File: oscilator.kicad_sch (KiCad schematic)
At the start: 5 parts, among them Y1 8Mhz

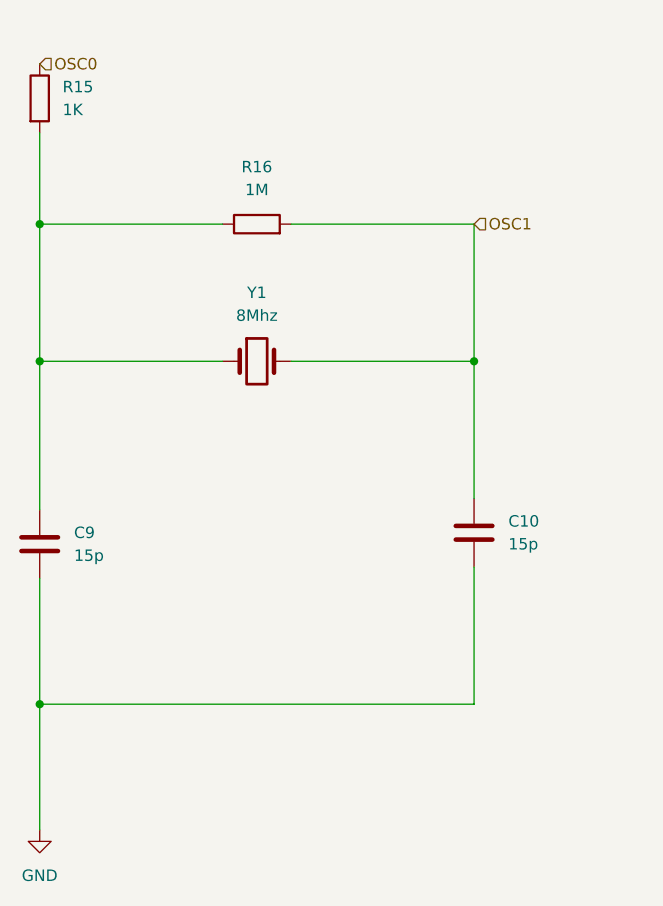
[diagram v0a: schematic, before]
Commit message: feat: PCB layout updates, schematic changes, fp-lib-table config
- cnc_pic32.kicad_pcb: component repositioning, board outline, text formatting
- cnc_pic32.kicad_prl/pro: project settings updates
- fp-lib-table: add Library path to Library.pretty
- mcu.kicad_sch: PIC32 pin configuration updates
- zigbee.kicad_sch: MRF24J40 module updates
- oscilator.kicad_sch: crystal configuration
- power.kicad_sch/power_ft232.kicad_sch: power supply updates
- oled.kicad_sch: OLED display connections
- idc.kicad_sch: IDC connector updates
- osc_ft232.kicad_sch: FT232 crystal
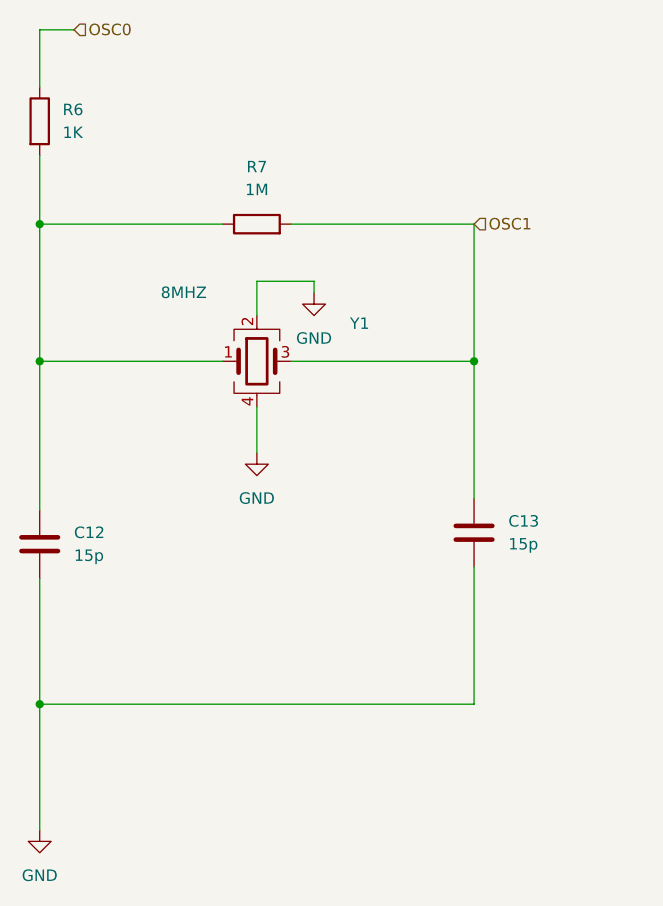
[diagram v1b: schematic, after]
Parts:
- removed Y1: 8Mhz, symbol Device:Crystal
- added Y1: 8MHZ, Crystal:Crystal_SMD_0603-4Pin_6.0x3.5mm, symbol Device:Crystal_GND24
- renumbered C9 to C12, C10 to C13, R15 to R6, R16 to R7
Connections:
- net GND: now also Y1.2, Y1.4
- net OSC1: now also Y1.3
- net at C12.1, R6.2, R7.1: now also Y1.1
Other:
- moved on the sheet: R6

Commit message: feat: integrate zigbee sheet + R 0603→0805 footprint update
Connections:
- net OSC0 renamed OSC2
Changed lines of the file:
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@@
 	(paper "A4")
 	(junction
+		(at 127 125.73)
+		(diameter 0)
+		(color 0 0 0 0)
+	)
+	(junction
+		(at 127 72.39)
+		(diameter 0)
+		(color 0 0 0 0)
+	)
+	(junction
 		(at 175.26 87.63)
 		(diameter 0)
@@
 	)
 	(junction
-		(at 127 125.73)
-		(diameter 0)
-		(color 0 0 0 0)
-	)
-	(junction
-		(at 127 72.39)
+		(at 175.26 72.39)
 		(diameter 0)
 		(color 0 0 0 0)
@@
 	(wire
 		(pts
+			(xy 175.26 62.23) (xy 175.26 72.39)
+		)
+		(stroke
+			(width 0)
+			(type default)
+		)
+	)
+	(wire
+		(pts
 			(xy 127 125.73) (xy 175.26 125.73)
 		)
@@
 		(pts
 			(xy 130.81 50.8) (xy 127 50.8)
+		)
+		(stroke
+			(width 0)
+			(type default)
+		)
+	)
+	(wire
+		(pts
+			(xy 175.26 62.23) (xy 186.69 62.23)
 		)
 		(stroke
@@
 	(hierarchical_label "OSC1"
 		(shape input)
-		(at 175.26 72.39 0)
+		(at 186.69 62.23 0)
 		(effects
 			(font
@@
 		)
 	)
-	(hierarchical_label "OSC0"
+	(hierarchical_label "OSC2"
 		(shape input)
 		(at 130.81 50.8 0)
